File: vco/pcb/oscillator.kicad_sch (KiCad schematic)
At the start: 60 parts

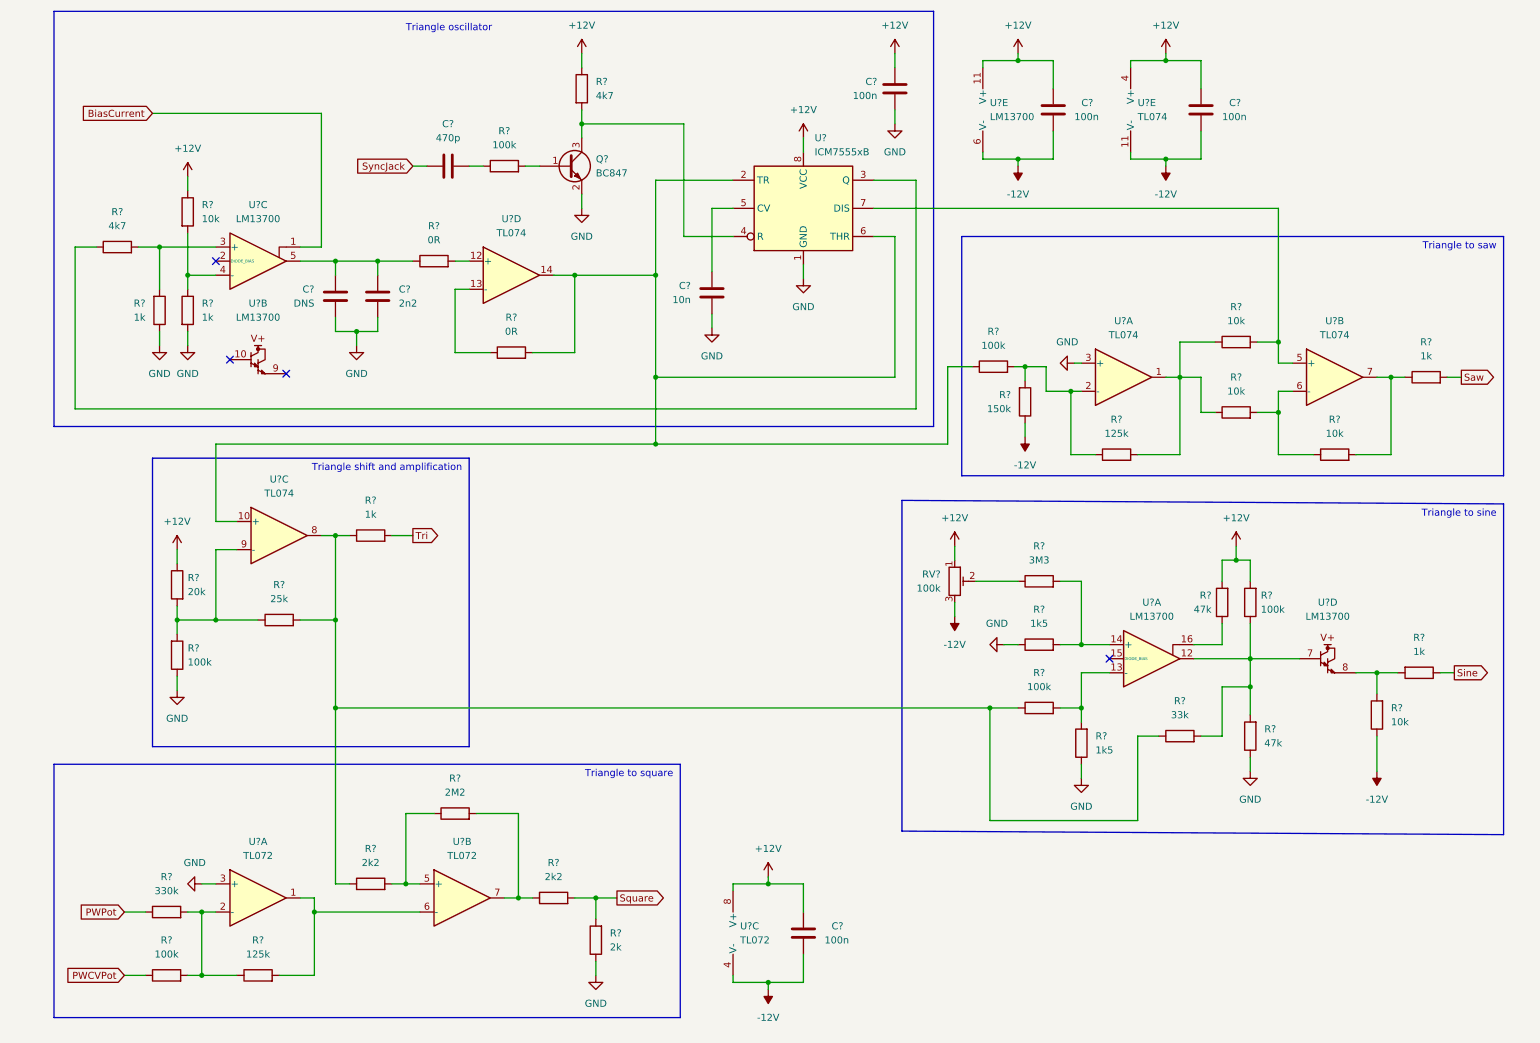
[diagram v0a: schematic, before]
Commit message: vco: Schematic update, footprints
- small changes to the schematic
- footprints assigned to all parts
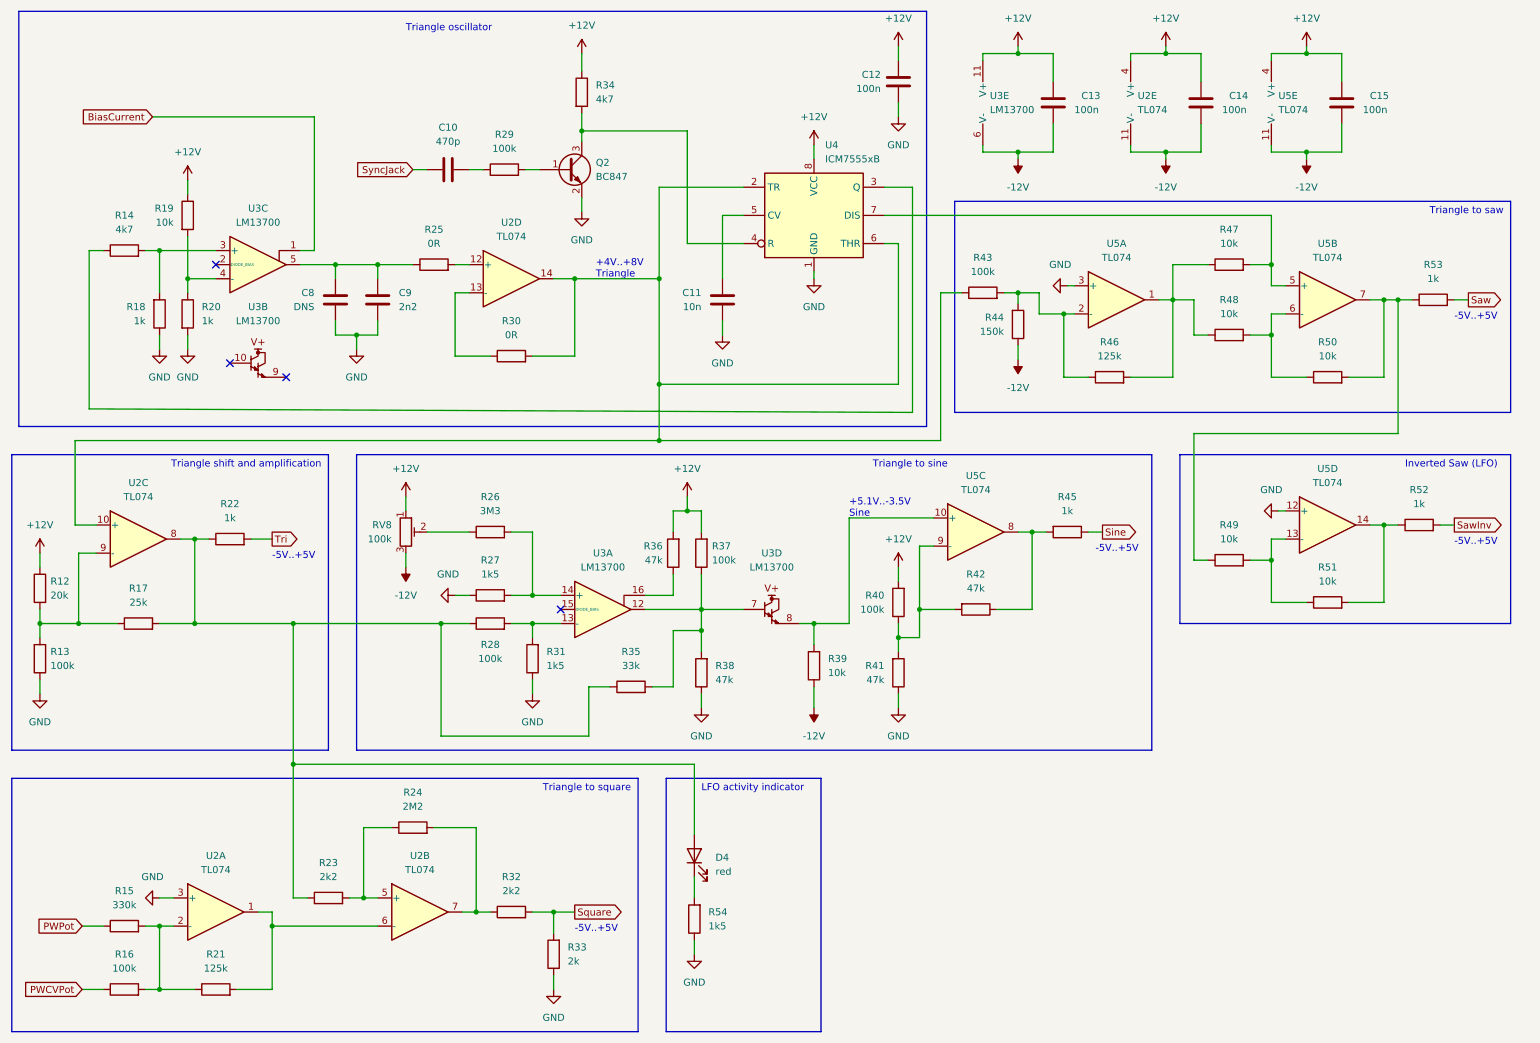
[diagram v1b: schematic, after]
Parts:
- removed C?: 100n, symbol Device:C
- removed U? (x3): TL072, symbol Amplifier_Operational:TL072
- added C15: 100n, Capacitor_SMD:C_0603_1608Metric_Pad1.08x0.95mm_HandSolder, symbol Device:C
- added D4: red, LED_THT:LED_D3.0mm_FlatTop, symbol Device:LED
- added R40: 100k, Resistor_SMD:R_0603_1608Metric_Pad0.98x0.95mm_HandSolder, symbol Device:R
- added R41, R42: 47k, Resistor_SMD:R_0603_1608Metric_Pad0.98x0.95mm_HandSolder, symbol Device:R
- added R49, R51: 10k, Resistor_SMD:R_0603_1608Metric_Pad0.98x0.95mm_HandSolder, symbol Device:R
- added R52: 1k, Resistor_SMD:R_0603_1608Metric_Pad0.98x0.95mm_HandSolder, symbol Device:R
- added R54: 1k5, Resistor_SMD:R_0603_1608Metric_Pad0.98x0.95mm_HandSolder, symbol Device:R
- added unit 1 of U2
- added unit 2 of U2
- added unit 3 of U5
- added unit 5 of U5
- added unit 4 of U5
- C10, C11, C12, C13, C14, C8, C9: renamed from C?; footprint (none) -> Capacitor_SMD:C_0603_1608Metric_Pad1.08x0.95mm_HandSolder
- Q2: renamed from Q?; footprint Package_TO_SOT_SMD:SOT-23 -> Package_TO_SOT_SMD:SOT-23_Handsoldering
- R12, R13, R14, R15, R16, R17, R18, R19, R20, R21, R22, R23, R24, R25, R26, R27, R28, R29, R30, R31, R32, R33, R34, R35, R36, R37, R38, R39, R43, R44, R45, R46, R47, R48, R50, R53: renamed from R?; footprint (none) -> Resistor_SMD:R_0603_1608Metric_Pad0.98x0.95mm_HandSolder
- RV8: renamed from RV?; footprint (none) -> Potentiometer_THT:Potentiometer_Bourns_3296W_Vertical
- U2, U5: renamed from U?; footprint (none) -> Package_SO:SOIC-14_3.9x8.7mm_P1.27mm
- U3: renamed from U?; footprint (none) -> Package_SO:SOIC-16_3.9x9.9mm_P1.27mm
- gave numbers to parts that had none: 1
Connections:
- net +12V: now also C15.1, R40.2, U5.4 (V+)
- net -12V: now also C15.2, U5.11 (V-)
- net GND: now also R41.1, R54.1, U2.3 (+), U5.12 (+)
- net at R17.2, R22.1, R23.1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: now also D4.2 (A)
- net at R50.2, R53.1, U5.7: now also R49.1
- net at R15.2, R16.2, R21.1: now also U2.2 (-)
- net at R39.2, U3.8: now also U5.10 (+); no longer R45.2
- net at R23.2, R24.1: now also U2.5 (+)
- net at R24.2, R32.1: now also U2.7
- net at R21.2: now also U2.1, U2.6 (-)
- new net: R40.1, R41.2, R42.2, U5.9 (-)
- new net: R42.1, R45.2, U5.8
- new net: R49.2, R51.1, U5.13 (-)
- new net: R51.2, R52.1, U5.14
- new net: D4.1 (K), R54.2
- new net SawInv: R52.2
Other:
- note added: "+4V..+8V Triangle"
- note added: "+5.1V..-3.5V Sine"
- note added: "-5V..+5V"
- note added: "Inverted Saw (LFO)"
- note added: "LFO activity indicator"
- title: (none) -> Oscillator
- moved on the sheet: C10, C11, C12, C13, C14, C8, C9, Q2, R12, R13, R14, R15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

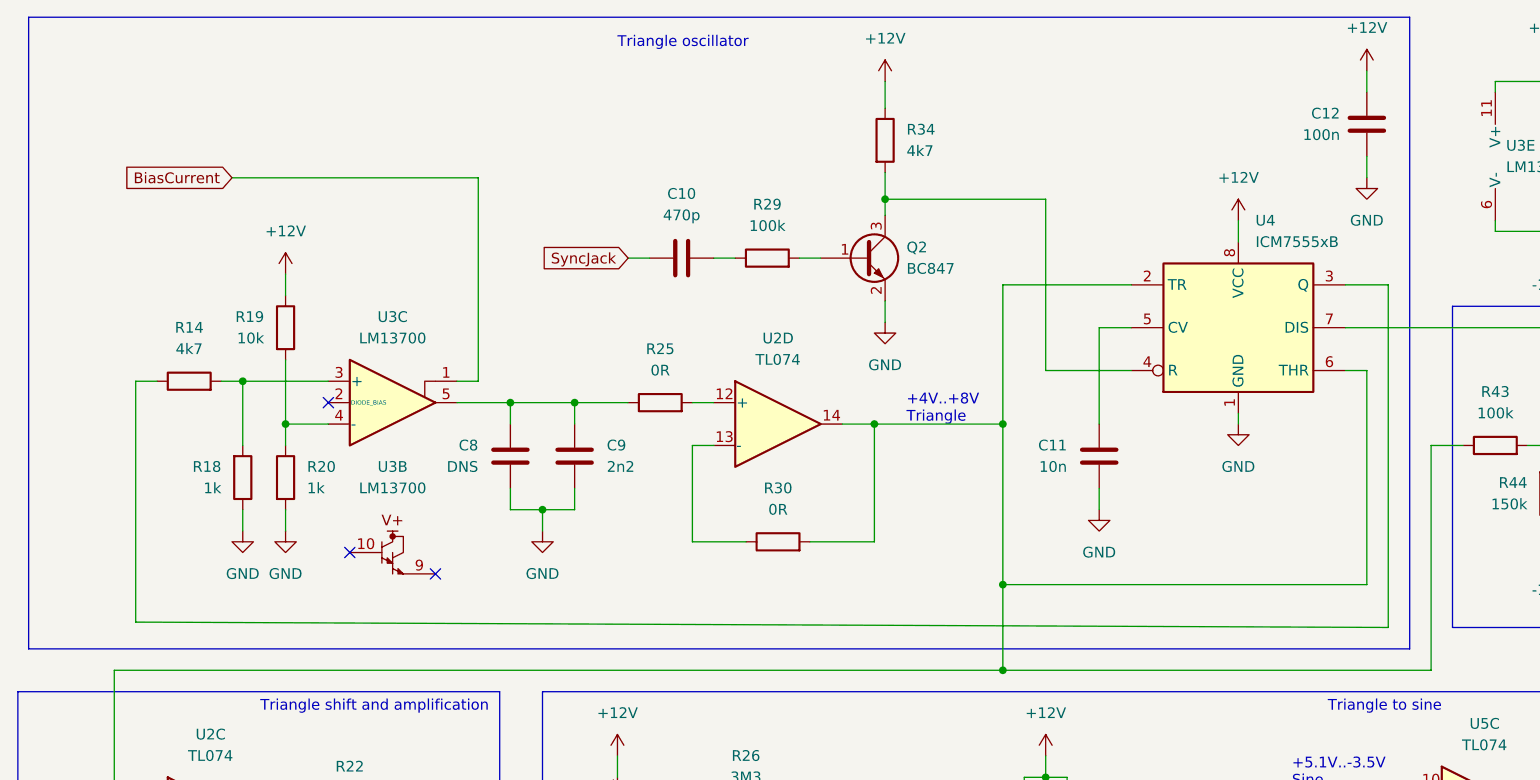
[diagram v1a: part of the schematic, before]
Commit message: vco: Add a VCO / LFO toggle switch
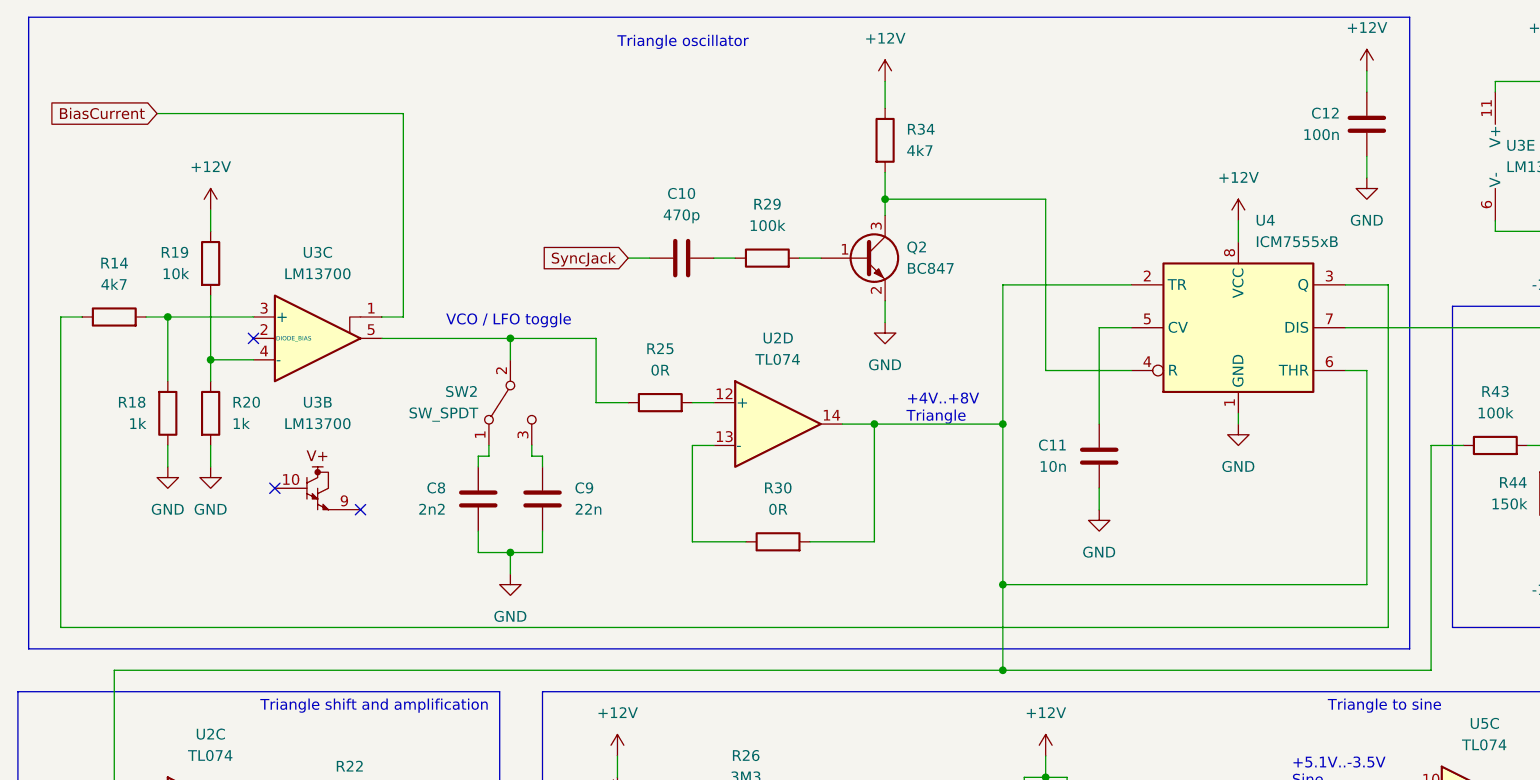
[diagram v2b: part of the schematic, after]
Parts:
- added SW2: SW_SPDT, Thonkiconn:Switch_Sub-Minitiature_Vertical, symbol Switch:SW_SPDT
- C8: value DNS -> 2n2
- C9: value 2n2 -> 22n
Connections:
- net at R25.1, U3.5: now also SW2.2 (B); no longer C8.2, C9.2
- new net: C8.2, SW2.1 (A)
- new net: C9.2, SW2.3 (C)
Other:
- note added: "VCO / LFO toggle"
- moved on the sheet: C8, C9, R14, R18, R19, R20, U3B, U3C

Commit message: vco: Layout WIP: component placement
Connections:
- net at R43.2, R44.2, R46.1: now also U5.13 (-); no longer U5.2 (-)
- net at R46.2, R47.1, R48.1: now also U5.14; no longer U5.1
- net at R49.2, R51.1: now also U5.2 (-); no longer U5.13 (-)
- net at R51.2, R52.1: now also U5.1; no longer U5.14
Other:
- moved on the sheet: U5A, U5D
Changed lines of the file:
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@@
     (pin "2")
   )
-  (symbol (lib_id "Amplifier_Operational:TL074") (at 251.46 105.41 0) (unit 4)
+  (symbol (lib_id "Amplifier_Operational:TL074") (at 213.36 64.77 0) (unit 4)
     (in_bom yes) (on_board yes) (fields_autoplaced)
-    (property "Reference" "U5" (id 0) (at 251.46 95.25 0))
-    (property "Value" "TL074" (id 1) (at 251.46 97.79 0))
-    (property "Footprint" "Package_SO:SOIC-14_3.9x8.7mm_P1.27mm" (id 2) (at 250.19 102.87 0)
+    (property "Reference" "U5" (id 0) (at 213.36 54.61 0))
+    (property "Value" "TL074" (id 1) (at 213.36 57.15 0))
+    (property "Footprint" "Package_SO:SOIC-14_3.9x8.7mm_P1.27mm" (id 2) (at 212.09 62.23 0)
       (effects (font (size 1.27 1.27)) hide)
     )
-    (property "Datasheet" "http://www.ti.com/lit/ds/symlink/tl071.pdf" (id 3) (at 252.73 100.33 0)
+    (property "Datasheet" "http://www.ti.com/lit/ds/symlink/tl071.pdf" (id 3) (at 214.63 59.69 0)
       (effects (font (size 1.27 1.27)) hide)
     )
@@
     (pin "2")
   )
-  (symbol (lib_id "Amplifier_Operational:TL074") (at 213.36 64.77 0) (unit 1)
+  (symbol (lib_id "Amplifier_Operational:TL074") (at 251.46 105.41 0) (unit 1)
     (in_bom yes) (on_board yes) (fields_autoplaced)
-    (property "Reference" "U5" (id 0) (at 213.36 54.61 0))
-    (property "Value" "TL074" (id 1) (at 213.36 57.15 0))
-    (property "Footprint" "Package_SO:SOIC-14_3.9x8.7mm_P1.27mm" (id 2) (at 212.09 62.23 0)
+    (property "Reference" "U5" (id 0) (at 251.46 95.25 0))
+    (property "Value" "TL074" (id 1) (at 251.46 97.79 0))
+    (property "Footprint" "Package_SO:SOIC-14_3.9x8.7mm_P1.27mm" (id 2) (at 250.19 102.87 0)
       (effects (font (size 1.27 1.27)) hide)
     )
-    (property "Datasheet" "http://www.ti.com/lit/ds/symlink/tl071.pdf" (id 3) (at 214.63 59.69 0)
+    (property "Datasheet" "http://www.ti.com/lit/ds/symlink/tl071.pdf" (id 3) (at 252.73 100.33 0)
       (effects (font (size 1.27 1.27)) hide)
     )
